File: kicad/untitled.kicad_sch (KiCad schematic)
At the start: 2 parts, among them U1 TLC5916IN

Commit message: added controller
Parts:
- added R1: 1.4 kΩ, symbol Device:R_US
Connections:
- net GND: now reaches U1.1 (GND)
- net GND: now also R1.1
- net at U1.15 (R-EXT): now also R1.2
- net +3V3: now reaches U1.16 (VDD)
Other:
- moved on the sheet: U1, U2

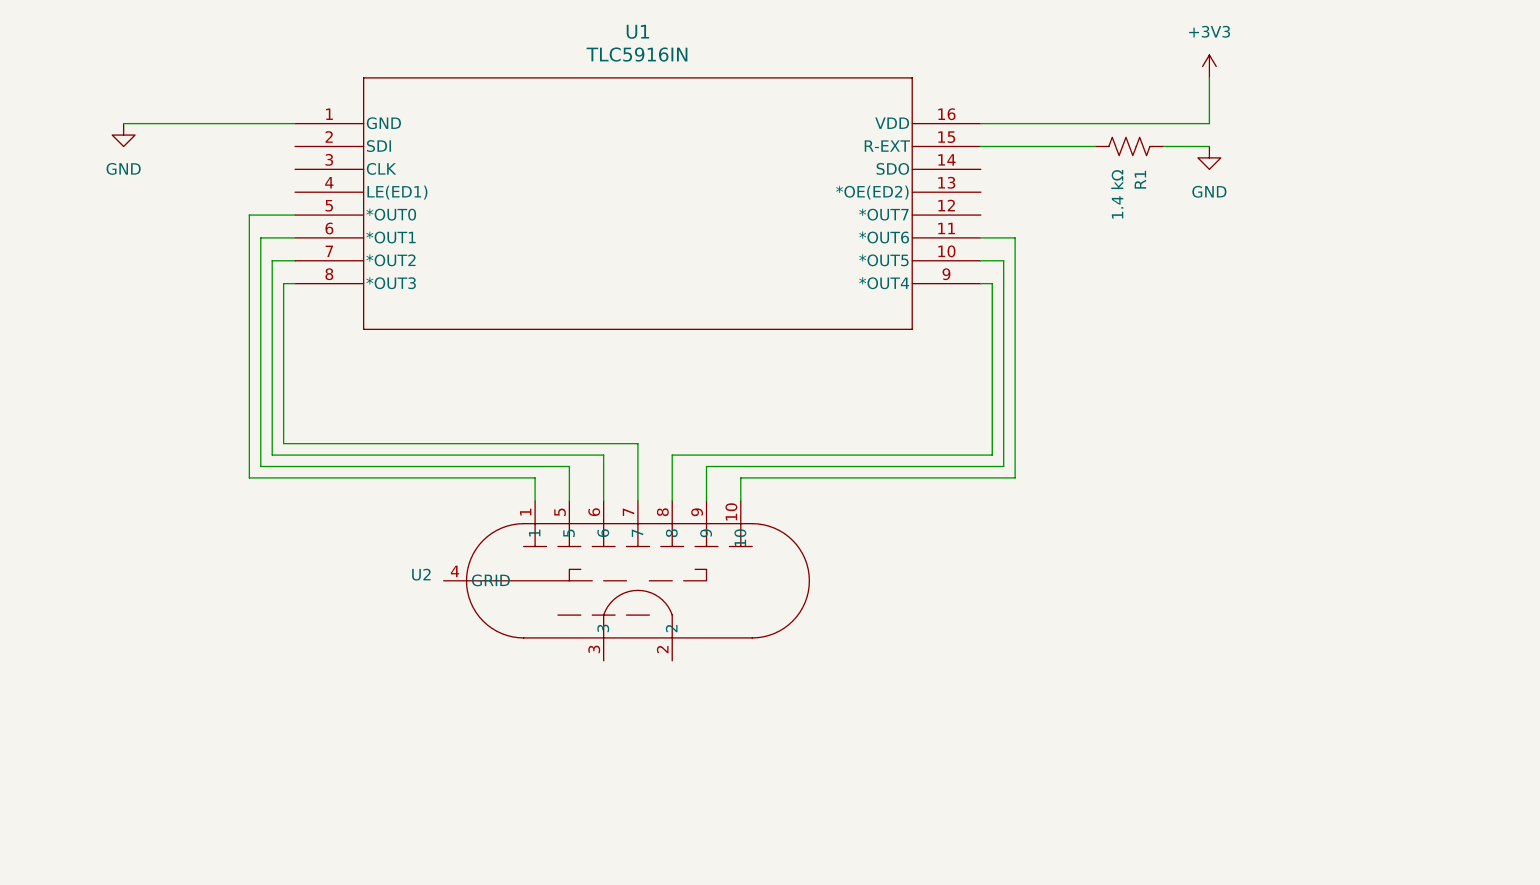
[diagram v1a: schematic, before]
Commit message: shift register wiring cleanup
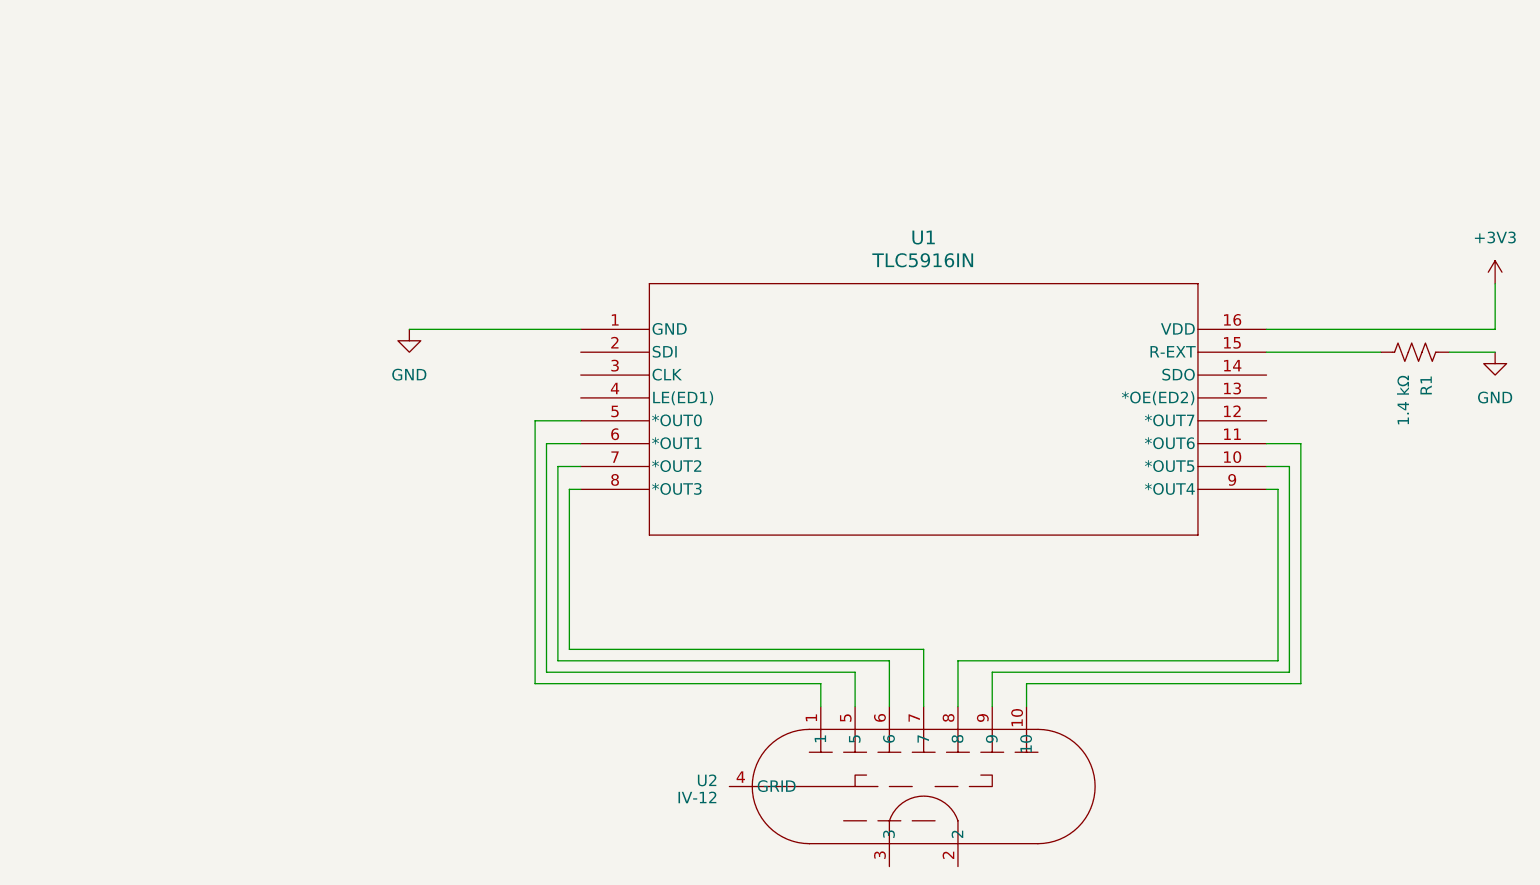
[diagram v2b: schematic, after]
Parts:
- U2: value ~ -> IV-12
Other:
- moved on the sheet: R1, U1, U2
